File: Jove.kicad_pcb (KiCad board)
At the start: 2 copper layers, 65 x 100 mm, 156 parts, among them J1 PJ301B, J2 PJ301B, J3 PJ301B, J4 PJ301B, J5 PJ301B, J6 PJ301B, P1 CONN_02X05, Q1 BCM857BS, Q2 BCM857BS, Q3 J112, Q4 J112, Q5 J112, Q6 J112, SW1 KS-01Q, U1 TL072-, U10 CD4027, U11 CD40106, U12 TS321, U13 TS321, U2 TL072-, U3 TL072-, U4 TL072-, U5 LM13700, U6 LM13700, U7 LM13700, U8 DG409, U9 CD4052

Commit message: redesign PCB
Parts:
- removed D4: LED, MyModules:3MM-LED-C1A2
- removed D7: 1N914, MyModules:SOD323-C1A2
- removed the REF** at (15.0, 15.0)
- removed the REF** at (74.5, 109.5)
- removed REF***: OSHW-Symbol_6.7x6mm_SilkScreen, Symbols:OSHW-Symbol_6.7x6mm_SilkScreen
- removed U11: CD40106, Housings_SSOP:TSSOP-14_4.4x5mm_Pitch0.65mm
- removed U13: TS321, TO_SOT_Packages_SMD:SOT-23-5
- added C30: 100n, Capacitor_SMD:C_0402_1005Metric, B.Cu at (36.8, 100.8)
- added C31: 100n, Capacitor_SMD:C_0402_1005Metric, B.Cu at (35.3, 106.7)
- added C32: 100n, Capacitor_SMD:C_0402_1005Metric, B.Cu at (32.4, 100.6)
- added G***: LOGO, LOGO, F.Cu at (-10.2, 59.4)
- added G***: LOGO, LOGO, F.Cu at (27.9, 59.4)
- added G***: LOGO, LOGO, F.Cu at (-12.8, 59.5)
- added J7: prog, Connector_PinHeader_2.54mm:PinHeader_1x04_P2.54mm_Vertical, B.Cu at (40.6, 70.5)
- added R79: 470k, Resistor_SMD:R_0603_1608Metric, B.Cu at (23.5, 18.2)
- added R80: 470k, Resistor_SMD:R_0603_1608Metric, B.Cu at (27.9, 14.5)
- added REF**: RK097_Drill_Hole_Panel, Genson_Drill_Holes:RK097_Drill_Hole_Panel, F.Cu at (-20.3, 45.7)
- added REF**: PJ392_Drill_Hole_Panel, Genson_Drill_Holes:PJ392_Drill_Hole_Panel, F.Cu at (-20.3, 76.2)
- added REF**: PJ392_Drill_Hole_Panel, Genson_Drill_Holes:PJ392_Drill_Hole_Panel, F.Cu at (-5.08, 91.4)
- added REF**: PJ392_Drill_Hole_Panel, Genson_Drill_Holes:PJ392_Drill_Hole_Panel, F.Cu at (-20.3, 91.4)
- added REF**: PJ392_Drill_Hole_Panel, Genson_Drill_Holes:PJ392_Drill_Hole_Panel, F.Cu at (-5.08, 76.2)
- added REF**: RK097_Drill_Hole_Panel, Genson_Drill_Holes:RK097_Drill_Hole_Panel, F.Cu at (-20.3, 61.0)
- added REF**: PJ392_Drill_Hole_Panel, Genson_Drill_Holes:PJ392_Drill_Hole_Panel, F.Cu at (-5.08, 106.7)
- added REF**: 6mm_cap_Drill_Hole_Panel, Genson_Drill_Holes:6mm_cap_Drill_Hole_Panel, F.Cu at (-12.7, 99.1)
- added REF**: PJ392_Drill_Hole_Panel, Genson_Drill_Holes:PJ392_Drill_Hole_Panel, F.Cu at (-20.3, 106.7)
- added REF**: LED_1.8mm_Drill_Hole_Panel, Genson_Drill_Holes:LED_1.8mm_Drill_Hole_Panel, F.Cu at (-4.83, 8.76)
- added REF**: RK097_Drill_Hole_Panel, Genson_Drill_Holes:RK097_Drill_Hole_Panel, F.Cu at (-12.7, 22.9)
- added REF**: 6HP_Front_Panel, Genson_Front_Panels:6HP_Front_Panel, F.Cu at (-27.9, -4.65)
- added REF**: RK097_Drill_Hole_Panel, Genson_Drill_Holes:RK097_Drill_Hole_Panel, F.Cu at (-5.08, 45.7)
- added REF**: LED_1.8mm_Drill_Hole_Panel, Genson_Drill_Holes:LED_1.8mm_Drill_Hole_Panel, F.Cu at (-1.02, 3.81)
- added REF**: RK097_Drill_Hole_Panel, Genson_Drill_Holes:RK097_Drill_Hole_Panel, F.Cu at (-5.08, 61.0)
- C1, C11, C2, C28, C29, C3, C4, C5, C8, C9: footprint MyModules:SM0603-C-JRL -> Capacitor_SMD:C_0603_1608Metric
- C10, C23, C24: footprint Capacitors_SMD:c_elec_5x5.3 -> Capacitor_Tantalum_SMD:CP_EIA-3216-18_Kemet-A
- C12, C13, C14, C15, C16, C17, C19, C20, C26, C27: footprint MyModules:SM0603-C-JRL -> Capacitor_SMD:C_0402_1005Metric
- C18, C25, C6, C7: footprint MyModules:CAP-BOX-PFR-5MM -> Capacitor_SMD:C_0603_1608Metric
- C21: value 0.47μ -> 330n; footprint MyModules:SM0603-C-JRL -> Capacitor_SMD:C_0603_1608Metric
- C22: value 0.47μ -> 100n; footprint MyModules:SM0603-C-JRL -> Capacitor_SMD:C_0402_1005Metric
- D1, D2: value LED -> red; footprint MyModules:3MM-LED-C1A2 -> LED_THT:LED_D1.8mm_W3.3mm_H2.4mm
- D10, D5, D6: footprint MyModules:SOD323-C1A2 -> Diode_SMD:D_SOD-323
- D3: value LED -> debug led; footprint MyModules:3MM-LED-C1A2 -> Diode_SMD:D_0603_1608Metric; moved to B.Cu
- D8, D9: value S1BB -> B5819WS; footprint MyModules:SMB-1C2A -> Diode_SMD:D_SOD-323
- J1: value PJ301B -> Resonance CV; footprint MyModules:PJ-301B-JACK-SLOTS -> Genson_Jacks:Jack_3.5mm_PJ392_Vertical
- J2: value PJ301B -> Bipolar Freq CV; footprint MyModules:PJ-301B-JACK-SLOTS -> Genson_Jacks:Jack_3.5mm_PJ392_Vertical
- J3: value PJ301B -> Unipolar Freq CV; footprint MyModules:PJ-301B-JACK-SLOTS -> Genson_Jacks:Jack_3.5mm_PJ392_Vertical
- J4, J5: value PJ301B -> Input2; footprint MyModules:PJ-301B-JACK-SLOTS -> Genson_Jacks:Jack_3.5mm_PJ392_Vertical
- J6: value PJ301B -> out; footprint MyModules:PJ-301B-JACK-SLOTS -> Genson_Jacks:Jack_3.5mm_PJ392_Vertical
- P1: footprint Pin_Headers:Pin_Header_Straight_2x05 -> Genson_Connectors:Eurorack_10Pin
- Q1, Q2: footprint SMD TRAN:sot323-6 -> Package_TO_SOT_SMD:SOT-363_SC-70-6
- Q3, Q4, Q5, Q6: footprint MyModules:SOT23-JRL -> Package_TO_SOT_SMD:SOT-23
- R1, R10, R11, R12, R13, R14, R15, R16, R17, R18, R2, R20, R22, R23, R24, R25, R26, R27, R29, R3, R30, R31, R32, R33, R34, R35, R36, R37, R38, R39, R4, R40, R42, R43, R44, R45, R46, R47, R48, R49, R5, R50, R51, R52, R53, R54, R55, R56, R57, R59, R6, R60, R62, R63, R64, R65, R68, R69, R7, R70, R71, R72, R73, R74, R75, R76, R77, R78, R8, R9: footprint MyModules:SM0603-R-JRL -> Resistor_SMD:R_0603_1608Metric
- R19: footprint MyModules:SM0805-HAND -> Resistor_SMD:R_0805_2012Metric
- R21, R28: value 1.5M -> 1M; footprint MyModules:SM0603-R-JRL -> Resistor_SMD:R_0603_1608Metric
- R41: value 3.3K -> 100k; footprint MyModules:SM0603-R-JRL -> Resistor_SMD:R_0603_1608Metric
- R58: value 33K -> 1k; footprint MyModules:SM0603-R-JRL -> Resistor_SMD:R_0603_1608Metric
- R61: value 100K -> 330; footprint MyModules:SM0603-R-JRL -> Resistor_SMD:R_0603_1608Metric
- R66, R67: footprint MyModules:SM0805-HAND -> Resistor_SMD:R_1206_3216Metric
- SW1: value KS-01Q -> SW_Push_DPDT; footprint synth:KS-01Q-02-JRL -> Genson_Switches:SW_5.8x5.8mm
- TP1, TP2: footprint MyModules:TEST POINT -> TestPoint:TestPoint_Pad_2.5x2.5mm; moved to F.Cu
- U1, U2, U3, U4: footprint MyModules:TSSOP8-JRL -> Package_SO:SOIC-8_3.9x4.9mm_P1.27mm
- U10: value CD4027 -> ~; footprint Housings_SSOP:TSSOP-16_4.4x5mm_Pitch0.65mm -> Package_SO:SOIC-8_3.9x4.9mm_P1.27mm
- U12: value TS321 -> TL072-; footprint TO_SOT_Packages_SMD:SOT-23-5 -> Package_SO:SOIC-8_3.9x4.9mm_P1.27mm
- U5, U6, U7, U8: footprint MyModules:SO16-JRL -> Package_SO:SOIC-16_3.9x9.9mm_P1.27mm
- U9: value CD4052 -> L78L05; footprint Housings_SSOP:TSSOP-16_4.4x5mm_Pitch0.65mm -> Package_TO_SOT_SMD:SOT-89-3
- VR1, VR2, VR3, VR4, VR6: footprint MyModules:RV16A-41-JRL -> Genson_Potentiometers:Potentiometer_RK09_RV09_Vertical
- VR5, VR7: footprint MyModules:TC33X-2 -> Potentiometer_SMD:Potentiometer_Bourns_TC33X_Vertical
- moved SW1 85.6 mm to (27.9, 99.1), turned to 90 degrees
- moved C26 84.2 mm to (36.3, 102.1)
- moved R58 72.2 mm to (32.0, 98.5)
- moved C19 71.4 mm to (16.3, 25.6)
- moved C27 63.3 mm to (23.9, 88.1), turned to 0 degrees
- moved R60 63.3 mm to (39.6, 15.0), turned to 0 degrees
- moved R64 61.1 mm to (16.0, 70.6), turned to 180 degrees
- moved R62 60.1 mm to (36.1, 15.0)
- moved C23 59.9 mm to (16.8, 38.4)
- moved D8 58.9 mm to (15.4, 34.7), turned to 90 degrees
- moved R8 56.9 mm to (20.3, 102.0)
- moved R66 55.7 mm to (17.9, 34.7), turned to 90 degrees
- moved U6 55.4 mm to (37.8, 21.4), turned to 0 degrees
- moved C20 55.1 mm to (33.3, 19.1), turned to -90 degrees
- moved R41 55.0 mm to (24.1, 65.0), turned to -90 degrees
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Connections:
- C2 pad 2: Net-(C2-Pad2) -> Net-(Q1-C1)
- C21 pad 1: Net-(C21-Pad1) -> +12V
- C22 pad 1: Net-(C22-Pad1) -> +5V
- C5 pad 2: Net-(C5-Pad2) -> Net-(Q2-C1)
- D1 pad 1: GND -> Net-(D1-K)
- D1 pad 2: Net-(D1-Pad2) -> /Rx
- D2 pad 1: GND -> Net-(D2-K)
- D2 pad 2: Net-(D2-Pad2) -> /Tx
- D3 pad 1: GND -> Net-(D3-K)
- D3 pad 2: Net-(D3-Pad2) -> Net-(D3-A)
- Q1 pad 6: Net-(C2-Pad2) -> Net-(Q1-C1)
- Q2 pad 6: Net-(C5-Pad2) -> Net-(Q2-C1)
- R21 pad 1: Net-(C2-Pad2) -> Net-(Q1-C1)
- R21 pad 2: -12V -> Net-(R21-Pad2)
- R28 pad 1: Net-(C5-Pad2) -> Net-(Q2-C1)
- R28 pad 2: -12V -> Net-(R28-Pad2)
- R4 pad 2: Net-(J1-Pad3) -> Net-(J1-PadT)
- R41 pad 1: +12V -> +5V
- R41 pad 2: Net-(R41-Pad2) -> Net-(U10-P3.3)
- R54 pad 1: Net-(J6-Pad3) -> Net-(J6-PadT)
- R58 pad 1: Net-(C21-Pad1) -> Net-(U10-P3.3)
- R58 pad 2: +12V -> Net-(R58-Pad2)
- R59 pad 1: Net-(R59-Pad1) -> Net-(D1-K)
- R59 pad 2: Net-(C22-Pad1) -> GND
- R61 pad 1: Net-(C22-Pad1) -> Net-(D2-K)
- R61 pad 2: +12V -> GND
- R64 pad 1: Net-(C21-Pad1) -> Net-(D3-K)
- R64 pad 2: Net-(R64-Pad2) -> GND
- R76 pad 2: Net-(J2-Pad3) -> Net-(J2-PadT)
- R8 pad 2: Net-(J5-Pad3) -> Net-(J5-PadT)
- SW1 pad 1: Net-(R64-Pad2) -> +5V
- SW1 pad 2: GND -> Net-(R58-Pad2)
- SW1 pad 3: (no net) -> GND
- SW1 pad 4: (no net) -> unconnected-(SW1-A-Pad4)
- U10 pad 1: Net-(U10-Pad1) -> Net-(U10-P5.4)
- U10 pad 2: Net-(U10-Pad13) -> +5V
- U10 pad 3: Net-(U10-Pad3) -> Net-(U10-P5.5)
- U10 pad 4: Net-(U10-Pad12) -> GND
- U10 pad 5: +12V -> /Rx
- U10 pad 6: +12V -> /Tx
- U10 pad 7: GND -> Net-(D3-A)
- U10 pad 8: GND -> Net-(U10-P3.3)
- U12 pad 1: Net-(C2-Pad1) -> Net-(C5-Pad1)
- U12 pad 2: -12V -> Net-(Q2-C1)
- U12 pad 4: Net-(C2-Pad2) -> -12V
- U12 pad 5: +12V -> GND
- U5 pad 15: Net-(U5-Pad15) -> unconnected-(U5-Pad15)
- U5 pad 2: Net-(U5-Pad2) -> unconnected-(U5-Pad2)
- U6 pad 15: Net-(U6-Pad15) -> unconnected-(U6-Pad15)
- U6 pad 2: Net-(U6-Pad2) -> unconnected-(U6-Pad2)
- U7 pad 15: Net-(U7-Pad15) -> unconnected-(U7-Pad15)
- U7 pad 2: Net-(U7-Pad2) -> unconnected-(U7-Pad2)
- U8 pad 1: Net-(U10-Pad1) -> Net-(U10-P5.4)
- U8 pad 16: Net-(U10-Pad15) -> Net-(U10-P5.5)
- U9 pad 1: Net-(D1-Pad2) -> +5V
- U9 pad 2: Net-(D3-Pad2) -> GND
- U9 pad 3: Net-(R41-Pad2) -> +12V
- VR3 pad 3: Net-(J2-Pad3) -> Net-(J2-PadT)
- VR4 pad 3: Net-(J3-Pad3) -> Net-(J3-PadT)
- VR6 pad 3: Net-(J4-Pad3) -> Net-(J4-PadT)
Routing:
- net +12V: track 500.1 -> 222.5 mm, vias 23 -> 19
- net -12V: track 340.1 -> 216.3 mm, vias 20 -> 22
- net Net-(U10-Pad1): track 94.4 -> 0.00 mm, vias 4 -> 0
- net Net-(U10-Pad15): track 81.0 -> 0.00 mm
- net /Rx: track 0.00 -> 79.0 mm, vias 0 -> 2
- net /Tx: track 0.00 -> 75.5 mm, vias 0 -> 3
- net Net-(J4-Pad3): track 74.2 -> 0.00 mm
- net Net-(U3A--): track 8.96 -> 82.2 mm, vias 0 -> 5
- net Net-(J2-Pad3): track 70.0 -> 0.00 mm
- net Net-(R3-Pad2): track 72.5 -> 2.98 mm, vias 1 -> 0
- net Net-(Q5-S): track 44.3 -> 112.2 mm, vias 0 -> 2
- net +5V: track 0.00 -> 65.3 mm, vias 0 -> 1
- net Net-(J5-Pad3): track 62.4 -> 0.00 mm, vias 1 -> 0
- net Net-(U1B--): track 6.48 -> 67.0 mm, vias 0 -> 3
- net Net-(J4-PadT): track 0.00 -> 60.3 mm, vias 0 -> 2
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- added copper zone on F.Cu, net (none)
- added copper zone on In1.Cu, net GND
- added copper zone on In2.Cu, net GND
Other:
- board size 65 x 100 mm -> 30.5 x 128.5 mm
- copper layers 2 -> 4
- net class Default removed
- net class POWER removed
- board text added: "+"
- board text added: "1V/oct"
- board text added: "50k lin"
- board text added: "50k log"
- board text added: "CV"
- board text added: "Q"
- board text removed: "-12V"
- board text removed: "CV 1 BI"
- board text removed: "CV 2 UNI"
- board text removed: "FREQ"
- board text removed: "FREQ ADJ"
- board text removed: "IN 1"
- board text removed: "IN 2"
- board text removed: "JOVE"
- board text removed: "LEVEL 2"
- board text removed: "M I M O I D"
- board text removed: "MODE"
- board text removed: "Multimode Filter v1.4 01 2017"
- board text removed: "OUT"
- board text removed: "RES"
- board text removed: "RES ADJ"
- board text removed: "RES CV"
- board text removed: "system80.net"

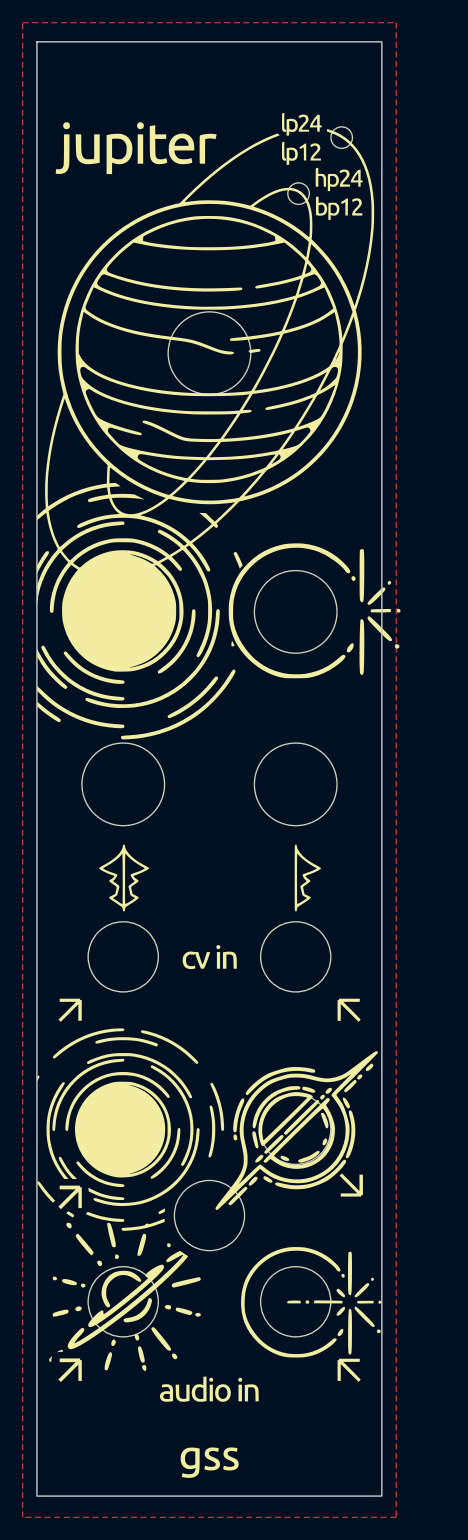
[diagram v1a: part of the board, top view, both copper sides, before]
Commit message: ordered fixed frontpanels
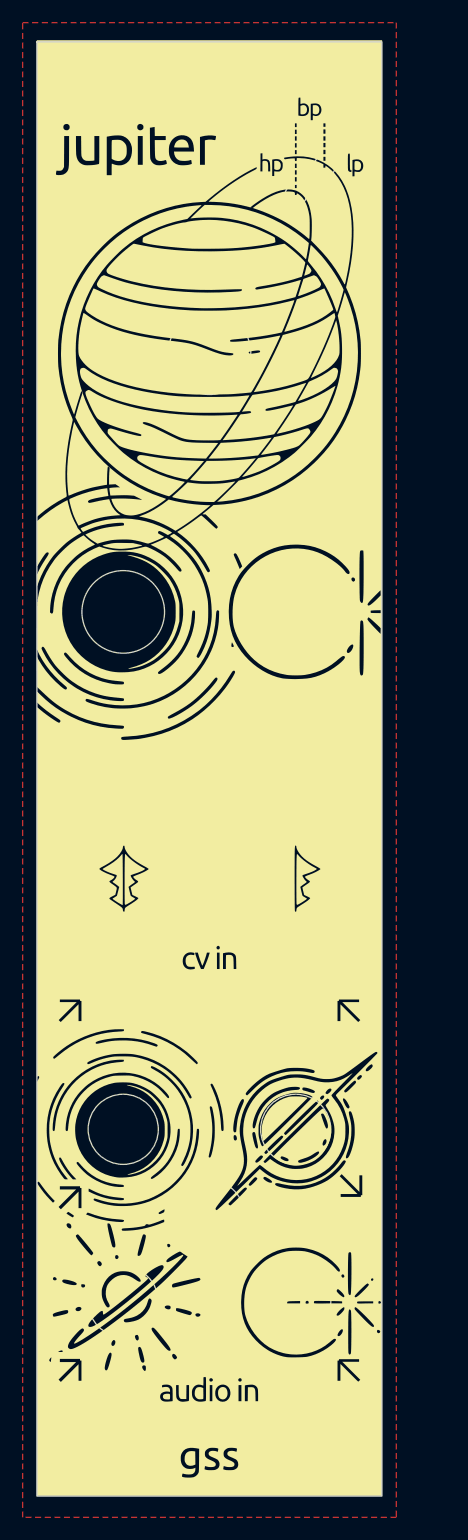
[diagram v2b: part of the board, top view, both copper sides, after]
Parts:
- moved REF** 2.96 mm to (-2.54, 6.35)
- moved G*** 2.54 mm to (-12.7, 59.5)
- moved REF** 0.28 mm to (-5.08, 8.89)

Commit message: add batch 2 changes
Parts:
- D10, D5, D6: value 1N914 -> 1N4148WS
- R12, R54: value 1K -> 1k
- R2, R24, R26, R3, R4, R44, R45, R47, R48, R7, R73, R74, R75, R76, R77, R78, R8: value 100K -> 100k
- R64: value 330 -> 1k
- R66, R67: value 10 -> PPTC
- U1, U12, U2, U3, U4: value TL072- -> TL072
- U10: value ~ -> STC8G1K08-36I
- VR1, VR2, VR3, VR4, VR6: value 50K -> 100k
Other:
- board text added: "100k lin"
- board text added: "100k log"
- board text added: "Q trim"
- board text added: "batch #"
- board text added: "cutoff"
- board text added: "id"
- board text added: "red stripe"
- board text added: "trim"
- board text added: "www.maxgenson.de/jupiter"
- board text removed: "50k lin"
- board text removed: "50k log"
